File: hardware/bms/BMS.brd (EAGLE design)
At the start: 97.8 x 86.4 mm, 124 parts, among them Q1 FDY102PZ, Q10 FDY102PZ, Q11 FDY102PZ, Q12 FDY102PZ, Q2 FDY102PZ, Q3 FDY102PZ, Q4 FDY102PZ, Q5 FDY102PZ, Q6 FDY102PZ, Q7 FDY102PZ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

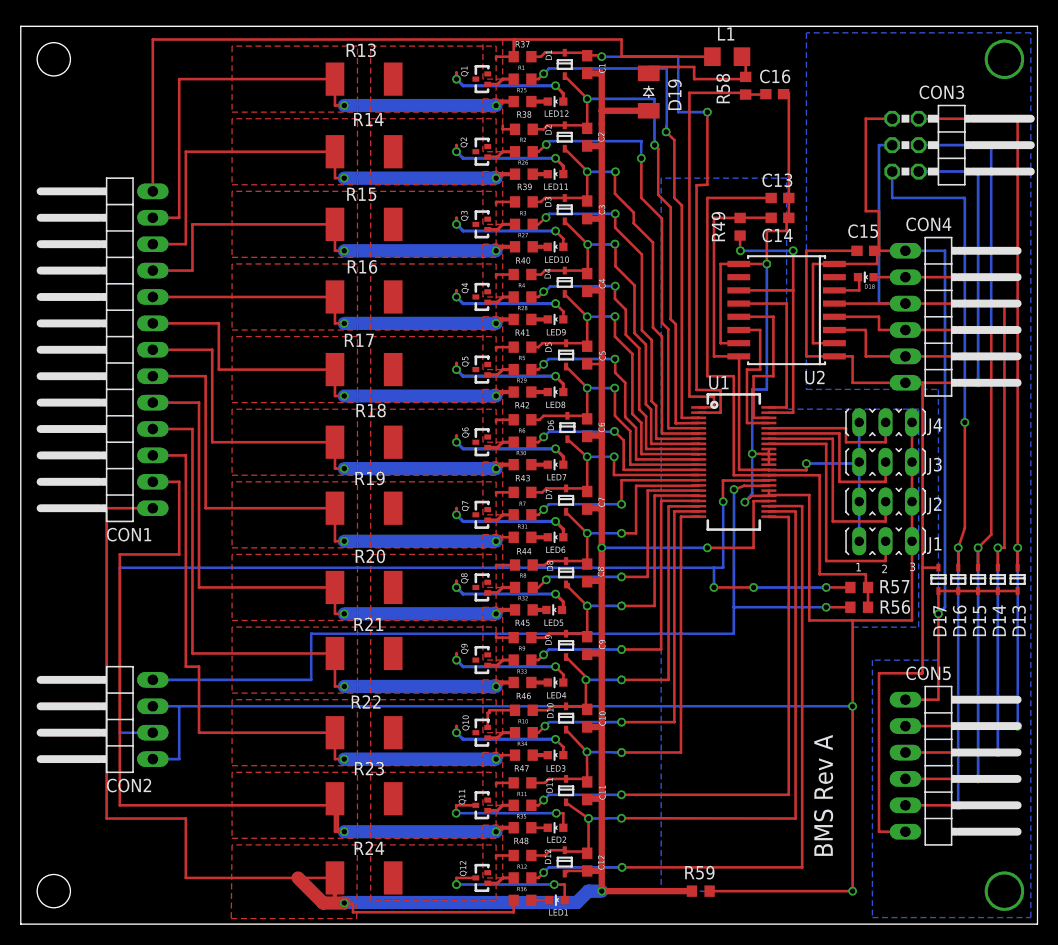
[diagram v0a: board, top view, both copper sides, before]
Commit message: Update ground planes, fix misc. route alignment, add decoupling capacitor for '1411. Add ESD protection diode array.
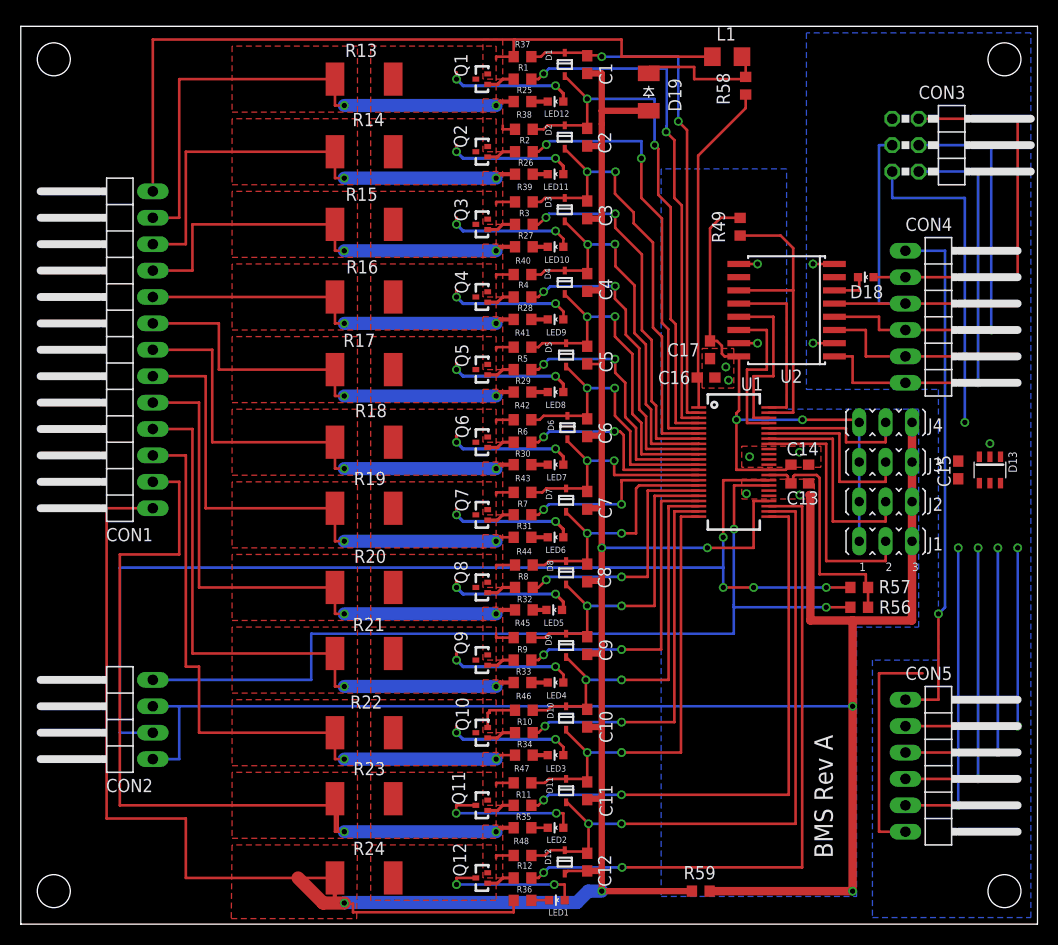
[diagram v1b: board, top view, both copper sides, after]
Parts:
- removed D14, D15, D16, D17: (no value), Richard1:SOD323
- added C17: 0.1uF, rcl:C0603
- C14: value 10uF -> 1uF
- C15: value 10uf -> 0.1u
- D13: device Richard1:SOD323 -> m_diode:SOT23-6
- moved C16 28.0 mm to (65.9, 52.6)
- moved C13 27.5 mm to (74.9, 42.4)
- moved C14 23.8 mm to (74.9, 44.2)
- moved C15 22.9 mm to (90.2, 43.7), turned to 90 degrees
- moved D13 9.77 mm to (93.2, 43.7), turned to 180 degrees
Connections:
- net N$100 renamed +VBAT
- net N$79 renamed VREF
- removed net N$88: C15.2, CON3.1, CON4.1, CON5.1, D13.P$2, D14.P$2, D15.P$2, D16.P$2, D17.P$2, U2.2, U2.8
- new net GND1: C15.2, CON3.1, CON4.1, CON5.1, D13.2, U2.2, U2.8
- net +5V: now also C17.1
- net GND: now also C17.2
- net N$57: now also D13.6; no longer D13.P$1
- net N$83: now also D13.4; no longer D16.P$1
- net N$85: now also D13.3; no longer D15.P$1
- net N$86: now also D13.1; no longer D14.P$1
- net N$90: now also D13.5; no longer D17.P$1
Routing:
- net N$88: track 96.8 -> 0.00 mm, vias 3 -> 0
- net GND: track 224.2 -> 159.4 mm, vias 5 -> 10
- net GND1: track 0.00 -> 54.5 mm, vias 0 -> 4
- net N$90: track 111.7 -> 64.4 mm
- net VREF: track 61.0 -> 23.2 mm
- net N$57: track 94.5 -> 66.6 mm
- net N$86: track 90.0 -> 64.0 mm
- net N$85: track 93.7 -> 70.3 mm
- net N$83: track 90.1 -> 76.0 mm
- net +VBAT: track 41.5 -> 32.4 mm
- net N$101: track 57.1 -> 50.3 mm
- net +5V: track 56.0 -> 58.0 mm, vias 1 -> 2
- net N$78: track 14.4 -> 15.7 mm
- net N$97: track 105.0 -> 104.0 mm
- net N$76: track 29.7 -> 29.0 mm, vias 2 -> 0
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- added copper zone on layer 1, net GND
- added copper zone on layer 16, net GND1
- removed copper zone on layer 16, net N$88

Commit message: BMS board SPI protected by a diode array in a single package and package labels adjusted to not touch tstop areas.
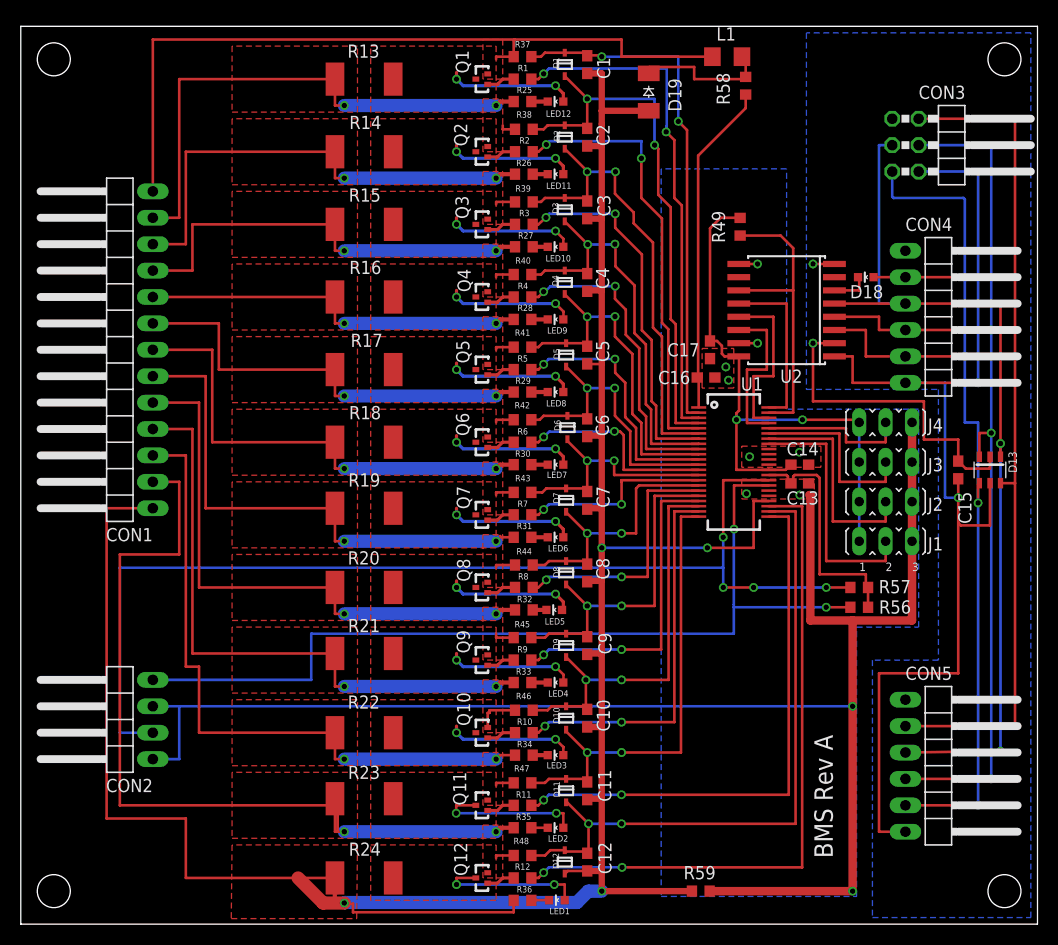
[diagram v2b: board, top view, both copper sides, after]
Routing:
- net N$90: track 64.4 -> 109.7 mm, vias 1 -> 2
- net N$57: track 66.6 -> 93.2 mm, vias 2 -> 0
- net N$85: track 70.3 -> 96.0 mm
- net N$86: track 64.0 -> 88.6 mm
- net GND1: track 54.5 -> 33.9 mm, vias 4 -> 2
- net N$83: track 76.0 -> 93.2 mm, vias 4 -> 3

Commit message: A couple of minor reroute changes to the layout
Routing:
- net GND1: track 33.9 -> 10.7 mm, vias 2 -> 3
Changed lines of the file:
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@@
 <wire x1="94.234" y1="59.69" x2="94.234" y2="46.228" width="0.254" layer="1"/>
 <wire x1="94.234" y1="46.228" x2="94.234" y2="44.958" width="0.254" layer="1"/>
-<wire x1="85.09" y1="16.51" x2="94.234" y2="16.637" width="0.254" layer="1"/>
-<via x="94.234" y="16.637" extent="1-16" drill="0.508"/>
-<wire x1="94.234" y1="16.637" x2="94.234" y2="46.228" width="0.254" layer="16"/>
+<wire x1="85.09" y1="16.51" x2="94.234" y2="16.51" width="0.254" layer="1"/>
+<via x="94.234" y="16.51" extent="1-16" drill="0.508"/>
+<wire x1="94.234" y1="16.51" x2="94.234" y2="46.228" width="0.254" layer="16"/>
 <wire x1="94.234" y1="46.355" x2="94.234" y2="46.228" width="0.254" layer="16"/>
 <via x="94.234" y="46.228" extent="1-16" drill="0.508"/>
@@
 <contactref element="C15" pad="2"/>
 <wire x1="90.17" y1="44.538" x2="90.17" y2="46.609" width="0.254" layer="1"/>
-<wire x1="90.17" y1="46.609" x2="86.868" y2="46.609" width="0.254" layer="1"/>
-<wire x1="86.868" y1="46.609" x2="86.868" y2="50.292" width="0.254" layer="1"/>
-<wire x1="86.868" y1="50.292" x2="76.2" y2="50.292" width="0.254" layer="1"/>
-<wire x1="76.2" y1="50.292" x2="76.2" y2="55.88" width="0.254" layer="1"/>
+<wire x1="90.17" y1="46.609" x2="90.1192" y2="46.609" width="0.254" layer="1"/>
+<wire x1="90.1192" y1="46.609" x2="86.868" y2="46.609" width="0" layer="19" extent="1-16"/>
+<wire x1="86.868" y1="46.609" x2="86.868" y2="50.292" width="0" layer="19" extent="1-16"/>
+<wire x1="86.868" y1="50.292" x2="76.2" y2="50.292" width="0" layer="19" extent="1-16"/>
+<wire x1="76.2" y1="50.292" x2="76.2" y2="55.88" width="0" layer="19" extent="1-16"/>
 <wire x1="93.218" y1="44.958" x2="93.218" y2="43.815" width="0.254" layer="1"/>
 <wire x1="93.218" y1="43.815" x2="90.893" y2="43.815" width="0.254" layer="1"/>
 <wire x1="90.893" y1="43.815" x2="90.17" y2="44.538" width="0.254" layer="1"/>
+<via x="90.1192" y="46.609" extent="1-16" drill="0.6"/>
 </signal>
 <signal name="N$89">

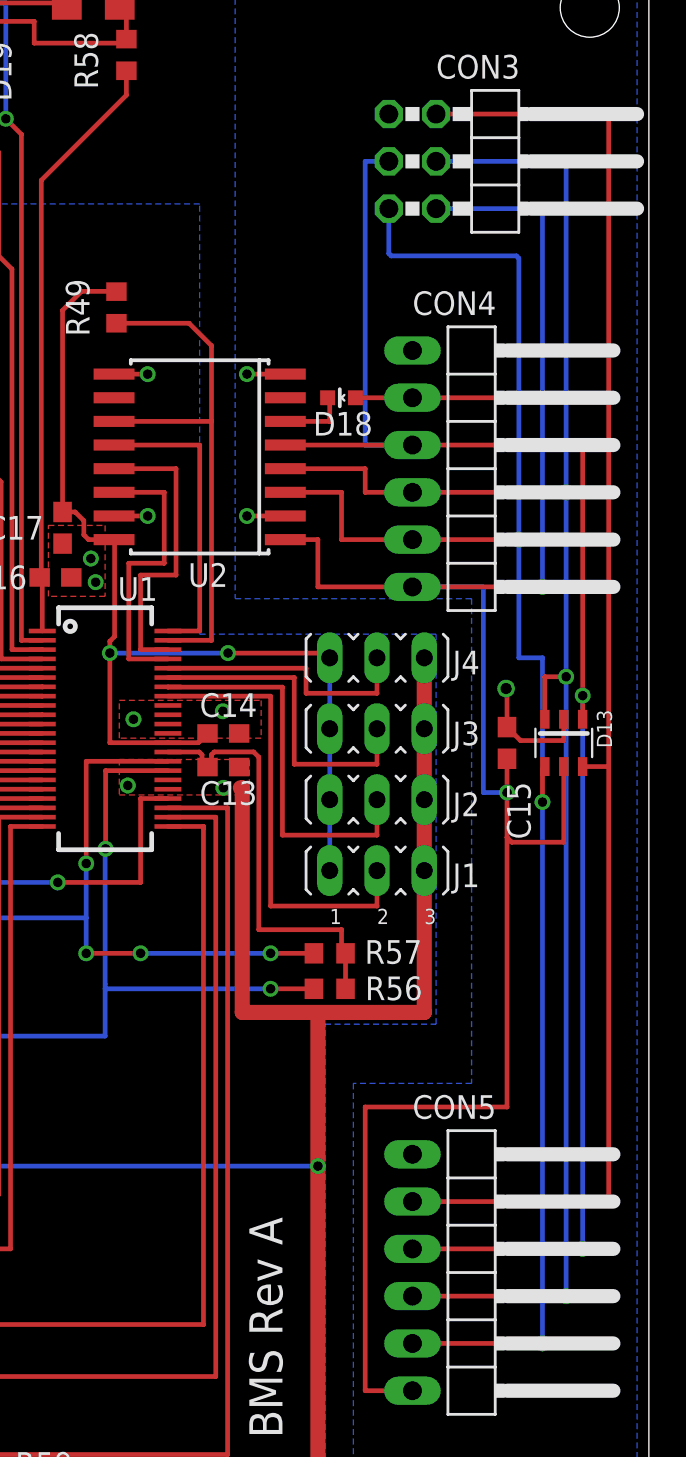
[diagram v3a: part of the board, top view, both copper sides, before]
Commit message: Move ESD suppression diode array between inputs and level shift IC. Add decoupling capacitor on level shift IC.
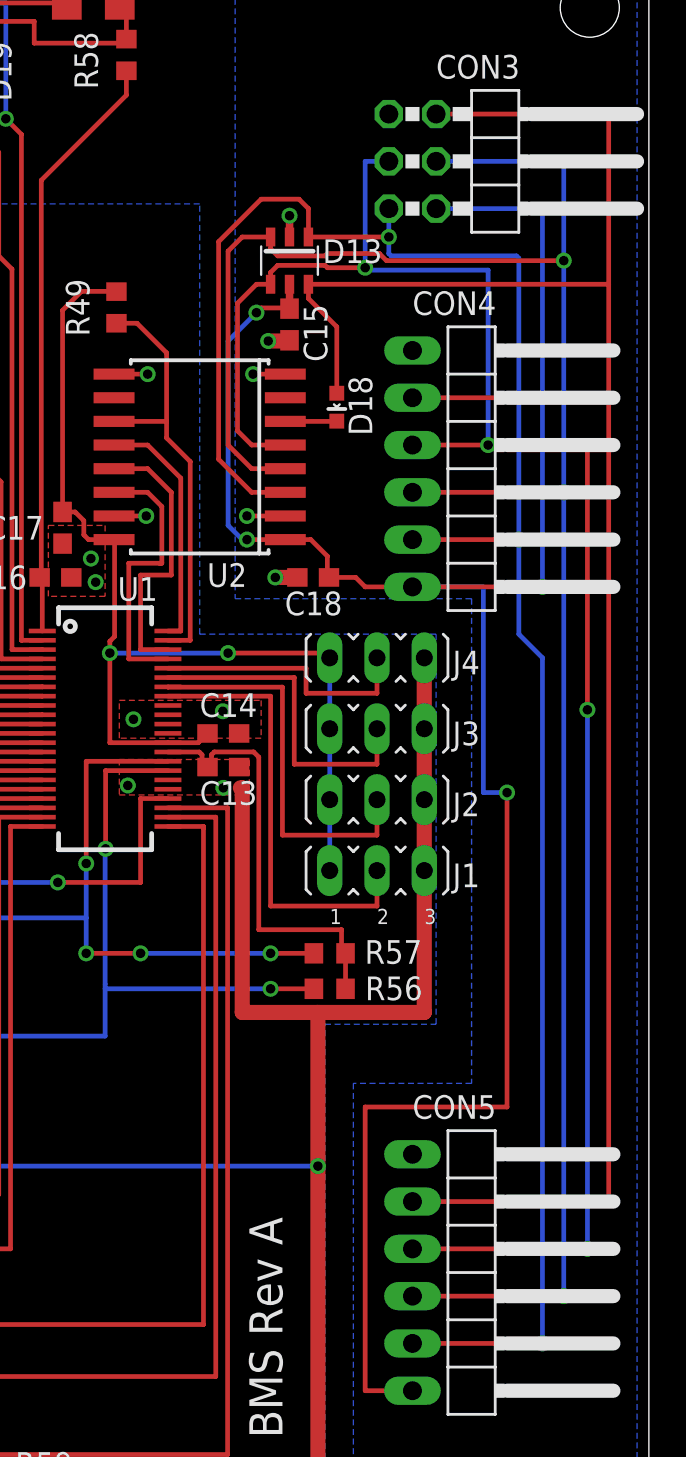
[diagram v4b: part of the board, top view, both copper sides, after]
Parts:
- added C18: 0.1uF, rcl:C0603
- moved D13 29.8 mm to (78.5, 69.6)
- moved C15 25.3 mm to (78.5, 66.2), turned to 270 degrees
- moved D18 0.57 mm to (81.0, 61.7), turned to 180 degrees
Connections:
- removed net N$90: C15.1, CON3.6, CON4.6, CON5.6, D13.5, U2.1
- new net VDD1: C15.1, C18.1, CON3.6, CON4.6, CON5.6, D13.5, U2.1
- net GND1: now also C18.2
- net N$83: now also D13.1; no longer D13.4
- net N$86: now also D13.4; no longer D13.1
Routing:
- net VDD1: track 0.00 -> 118.6 mm, vias 0 -> 4
- net N$90: track 109.7 -> 0.00 mm, vias 2 -> 0
- net N$85: track 96.0 -> 117.4 mm
- net N$57: track 93.2 -> 111.4 mm
- net N$83: track 93.2 -> 108.9 mm
- net N$86: track 88.7 -> 103.3 mm, vias 2 -> 4
- net N$76: track 29.0 -> 23.3 mm
- net GND1: track 10.7 -> 7.27 mm, vias 3 -> 5
- net N$75: track 16.3 -> 13.2 mm
- net N$77: track 16.4 -> 15.2 mm
- net N$89: track 3.77 -> 2.77 mm
- net N$78: track 15.7 -> 15.0 mm
